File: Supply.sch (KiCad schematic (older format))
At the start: 11 parts, among them P3 CONN_01X02, Q1 AO3401, U4 TPS79718, U5 EPL3015, U6 TPS61222

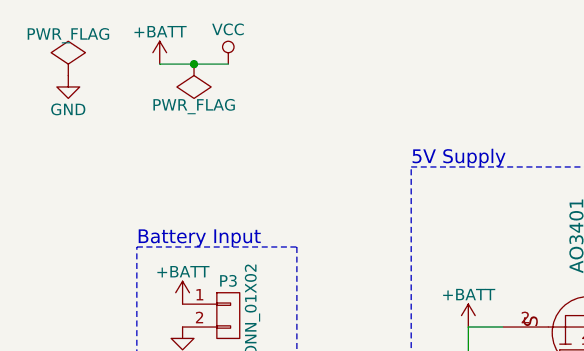
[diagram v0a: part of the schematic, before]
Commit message: Add prices
Signed-off-by: Philip Luyckx <philip.luyckx@gmail.com>
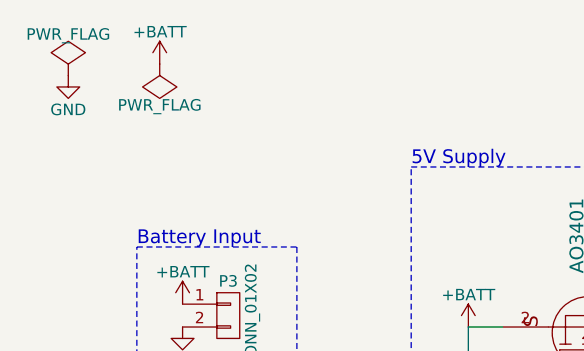
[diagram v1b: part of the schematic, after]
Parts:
- C17, C18: Price (none) -> 0.02
- P3: Price (none) -> 0.0
- R14: Price (none) -> 0.01
- U4: Price (none) -> 0.34
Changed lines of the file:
@@
 F 2 "PinHeaders:Pin_Header_Straight_1x02_TH" H 1800 2100 60  0001 C CNN
 F 3 "" H 1800 2100 60  0000 C CNN
+F 4 "0.0" H 1800 2100 60  0001 C CNN "Price"
 	1    1800 2100
 	1    0    0    -1
@@
 L PWR_FLAG #FLG043
 U 1 1 56635DC4
-P 1650 1000
-F 0 "#FLG043" H 1650 1095 50  0001 C CNN
-F 1 "PWR_FLAG" H 1650 1180 50  0000 C CNN
-F 2 "" H 1650 1000 60  0000 C CNN
-F 3 "" H 1650 1000 60  0000 C CNN
-	1    1650 1000
+P 1500 1000
+F 0 "#FLG043" H 1500 1095 50  0001 C CNN
+F 1 "PWR_FLAG" H 1500 1180 50  0000 C CNN
+F 2 "" H 1500 1000 60  0000 C CNN
+F 3 "" H 1500 1000 60  0000 C CNN
+	1    1500 1000
 	-1   0    0    1
 $EndComp
@@
 	3750 2000 3750 2150
 $Comp
-L VCC #PWR050
-U 1 1 5664A479
-P 1800 1000
-F 0 "#PWR050" H 1800 850 50  0001 C CNN
-F 1 "VCC" H 1800 1150 50  0000 C CNN
-F 2 "" H 1800 1000 60  0000 C CNN
-F 3 "" H 1800 1000 60  0000 C CNN
-	1    1800 1000
-	1    0    0    -1
-$EndComp
-Wire Wire Line
-	1500 1000 1800 1000
-Connection ~ 1650 1000
-$Comp
 L TPS61222 U6
 U 1 1 56687082
@@
 F 2 "CustomSmd:SC70" H 4200 4050 60  0001 C CNN
 F 3 "" H 4200 4050 60  0000 C CNN
+F 4 "0.34" H 4050 4000 60  0001 C CNN "Price"
 	1    4050 4000
 	-1   0    0    1
 $EndComp
 $Comp
-L +BATT #PWR051
+L +BATT #PWR050
 U 1 1 5752E781
 P 3500 3750
-F 0 "#PWR051" H 3500 3600 50  0001 C CNN
+F 0 "#PWR050" H 3500 3600 50  0001 C CNN
 F 1 "+BATT" H 3500 3890 50  0000 C CNN
 F 2 "" H 3500 3750 50  0000 C CNN
@@
 F 2 "Resistors_SMD:R_0805" H 3238 4000 50  0001 C CNN
 F 3 "" H 3200 4150 50  0000 C CNN
+F 4 "0.02" H 3200 4150 60  0001 C CNN "Price"
 	1    3200 4150
 	1    0    0    -1
 $EndComp
 $Comp
-L GND #PWR052
+L GND #PWR051
 U 1 1 5752E7D6
 P 3200 4300
-F 0 "#PWR052" H 3200 4050 50  0001 C CNN
+F 0 "#PWR051" H 3200 4050 50  0001 C CNN
 F 1 "GND" H 3200 4150 50  0000 C CNN
 F 2 "" H 3200 4300 50  0000 C CNN
@@
 $EndComp
 $Comp
-L GND #PWR053
+L GND #PWR052
 U 1 1 5752E81C
 P 4400 3850
-F 0 "#PWR053" H 4400 3600 50  0001 C CNN
+F 0 "#PWR052" H 4400 3600 50  0001 C CNN
 F 1 "GND" H 4400 3700 50  0000 C CNN
 F 2 "" H 4400 3850 50  0000 C CNN
@@
 F 2 "Resistors_SMD:R_0603" V 3830 4250 50  0001 C CNN
 F 3 "" H 3900 4250 50  0000 C CNN
+F 4 "0.01" V 3900 4250 60  0001 C CNN "Price"
 	1    3900 4250
 	0    1    1    0
@@
 F 2 "Resistors_SMD:R_0805" H 2888 4000 50  0001 C CNN
 F 3 "" H 2850 4150 50  0000 C CNN
+F 4 "0.02" H 2850 4150 60  0001 C CNN "Price"
 	1    2850 4150
 	1    0    0    -1
@@
 1V8 Supply\n
 $Comp
-L +1V8 #PWR054
+L +1V8 #PWR053
 U 1 1 5753ACA5
 P 3500 3950
-F 0 "#PWR054" H 3500 3800 50  0001 C CNN
+F 0 "#PWR053" H 3500 3800 50  0001 C CNN
 F 1 "+1V8" H 3500 4090 50  0000 C CNN
 F 2 "" H 3500 3950 50  0000 C CNN

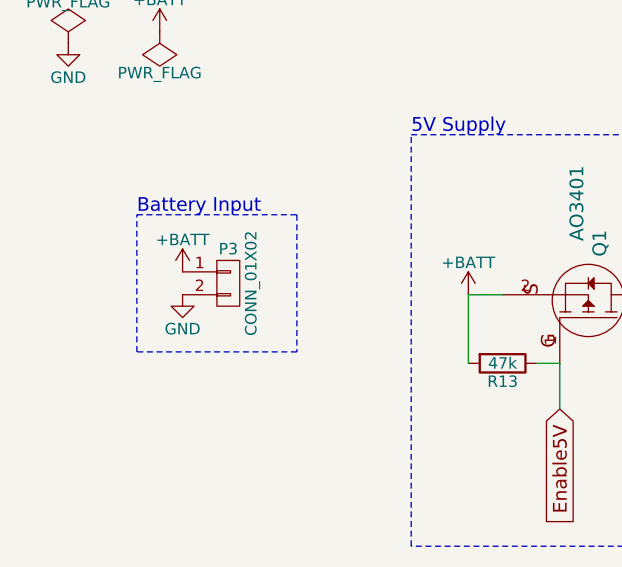
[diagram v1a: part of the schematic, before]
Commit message: Update connector for Vin
Signed-off-by: Philip Luyckx <philip.luyckx@gmail.com>
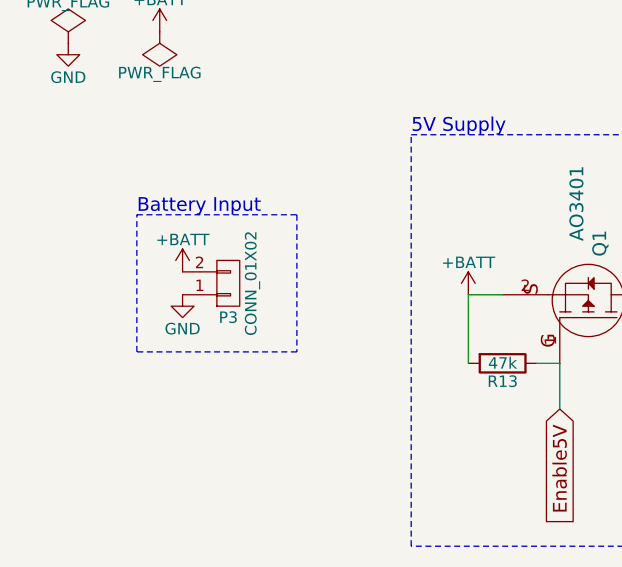
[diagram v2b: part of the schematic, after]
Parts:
- P3: footprint PinHeaders:Pin_Header_Straight_1x02_TH -> ConnWago:ConnWago_2059_2P_SMD; Price 0.0 -> 0.18
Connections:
- net +BATT: now also P3.2 (P2); no longer P3.1 (P1)
- net GND: now also P3.1 (P1); no longer P3.2 (P2)
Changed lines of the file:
@@
 F 0 "P3" H 1800 2250 50  0000 C CNN
 F 1 "CONN_01X02" V 1900 2100 50  0000 C CNN
-F 2 "PinHeaders:Pin_Header_Straight_1x02_TH" H 1800 2100 60  0001 C CNN
+F 2 "ConnWago:ConnWago_2059_2P_SMD" H 1800 2100 60  0001 C CNN
 F 3 "" H 1800 2100 60  0000 C CNN
-F 4 "0.0" H 1800 2100 60  0001 C CNN "Price"
+F 4 "0.18" H 1800 2100 60  0001 C CNN "Price"
 	1    1800 2100
-	1    0    0    -1
+	1    0    0    1
 $EndComp
 $Comp
